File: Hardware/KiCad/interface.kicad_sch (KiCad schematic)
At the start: 36 parts, among them J1 USB_C, J2 STLink, J6 UART, J7 OLED, SW10 SW_Push_45deg, SW11 SW_Push_45deg, SW12 SW_Push_45deg, SW13 SW_Push_45deg, SW14 SW_Push_45deg, SW15 SW_Push_45deg, SW16 SW_Push_45deg, SW17 SW_Push_45deg, SW18 Channel Select - ACZ11BRXE, SW2 SW_Push_45deg, SW3 SW_Push_45deg, SW4 SW_Push_45deg, SW5 SW_Push_45deg, SW6 SW_Push_45deg, SW7 SW_Push_45deg, SW8 SW_Push_45deg, SW9 SW_Push_45deg, U1 USBLC6-2

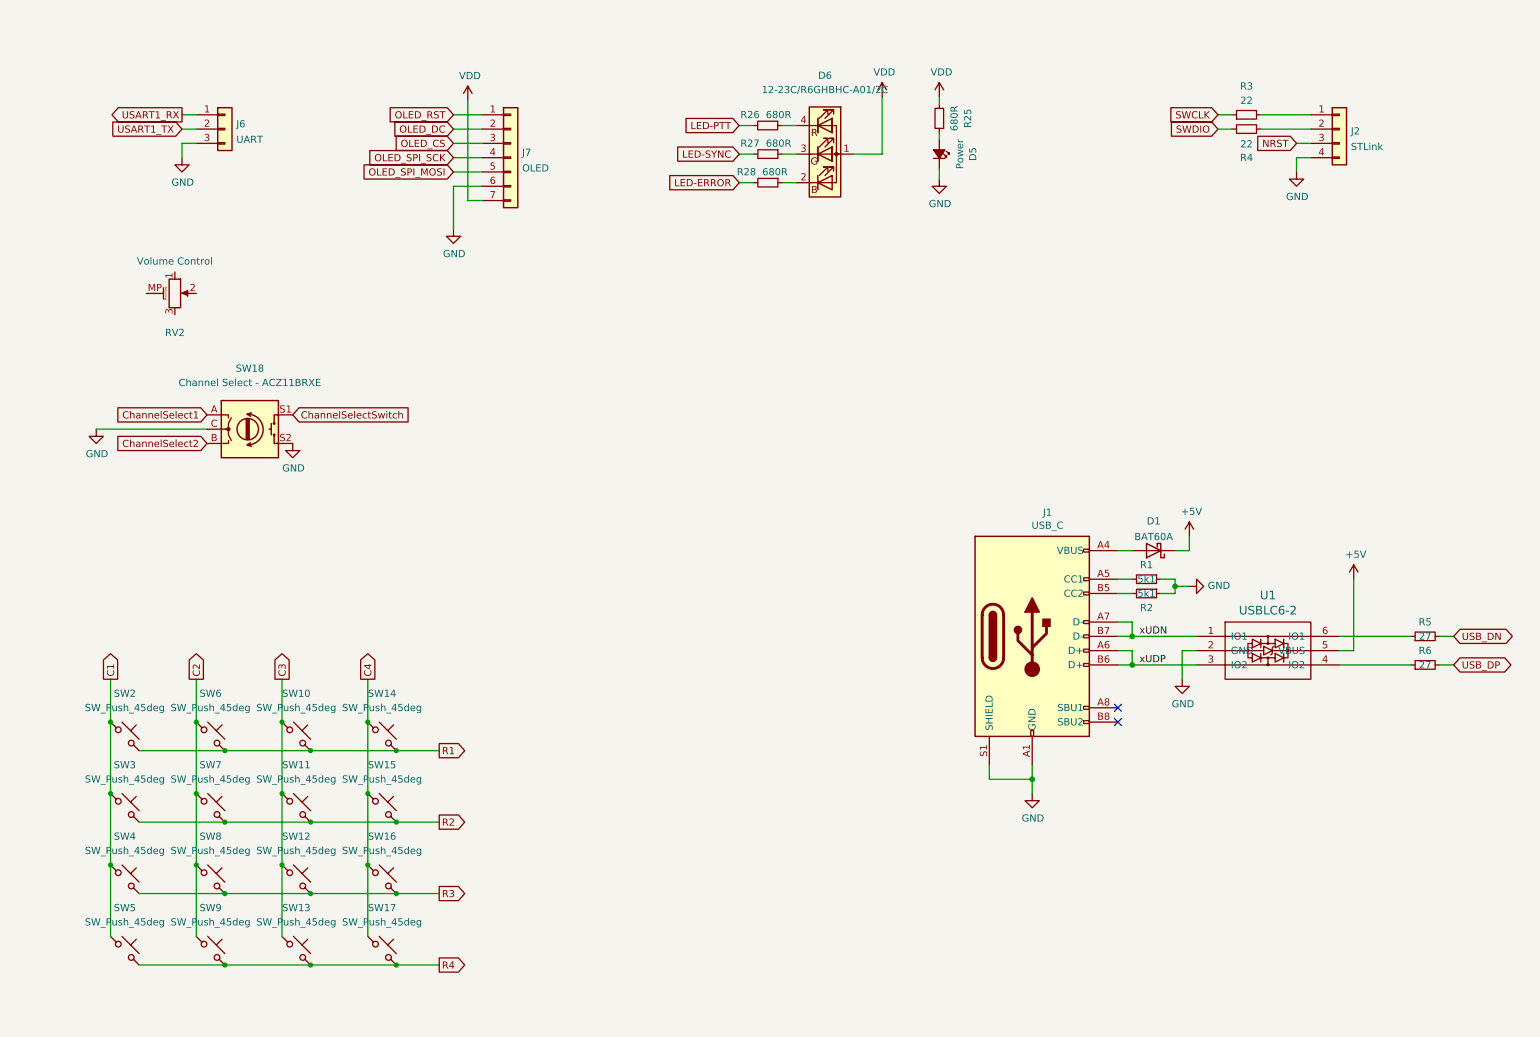
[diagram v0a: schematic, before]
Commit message: Schematic update
- nets for the internal speaker renamed
- encoder nets renamed, encoder circuit updated
- various other minor edits
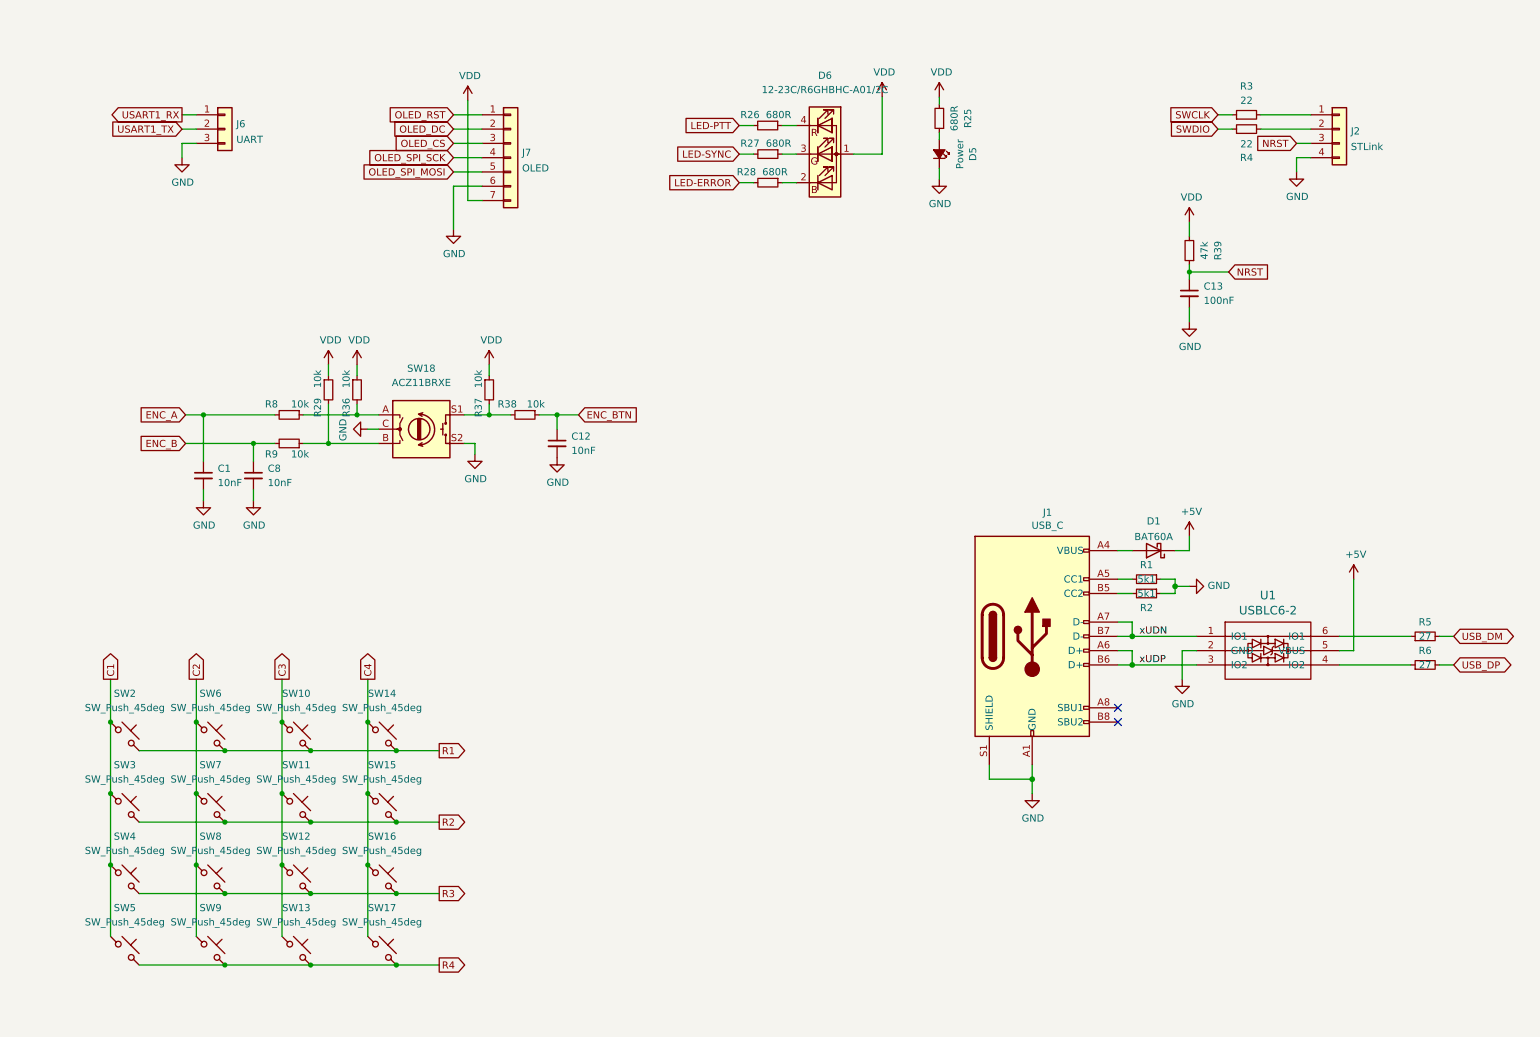
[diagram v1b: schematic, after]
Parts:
- removed RV2: Volume Control, Potentiometer_THT:Potentiometer_Alps_RK09L_Single_Horizontal, symbol Device:R_Potentiometer_MountingPin
- added C1, C12, C8: 10nF, Capacitor_SMD:C_0402_1005Metric, symbol Device:C_Small
- added C13: 100nF, Capacitor_SMD:C_0402_1005Metric, symbol Device:C_Small
- added R29, R36, R37, R38, R8, R9: 10k, Resistor_SMD:R_0402_1005Metric, symbol pkl_device:pkl_R_Small
- added R39: 47k, Resistor_SMD:R_0402_1005Metric, symbol pkl_device:pkl_R_Small
- SW18: value Channel Select - ACZ11BRXE -> ACZ11BRXE
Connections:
- net GND: now also C1.2, C12.2, C13.2, C8.2
- net NRST: now also C13.1, R39.1
- net VDD: now also R29.1, R36.1, R37.1, R39.2
- net ChannelSelect1: no longer names the net of SW18.A
- net ChannelSelect1: now also R36.2, R8.1
- net ChannelSelect2: no longer names the net of SW18.B
- net ChannelSelect2: now also R29.2, R9.1
- net ChannelSelectSwitch: no longer names the net of SW18.S1
- net ChannelSelectSwitch: now also R37.2, R38.2
- net USB_DN renamed USB_DM
- new net ENC_A: C1.1, R8.2
- new net ENC_B: C8.1, R9.2
- new net ENC_BTN: C12.1, R38.1
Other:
- moved on the sheet: SW18

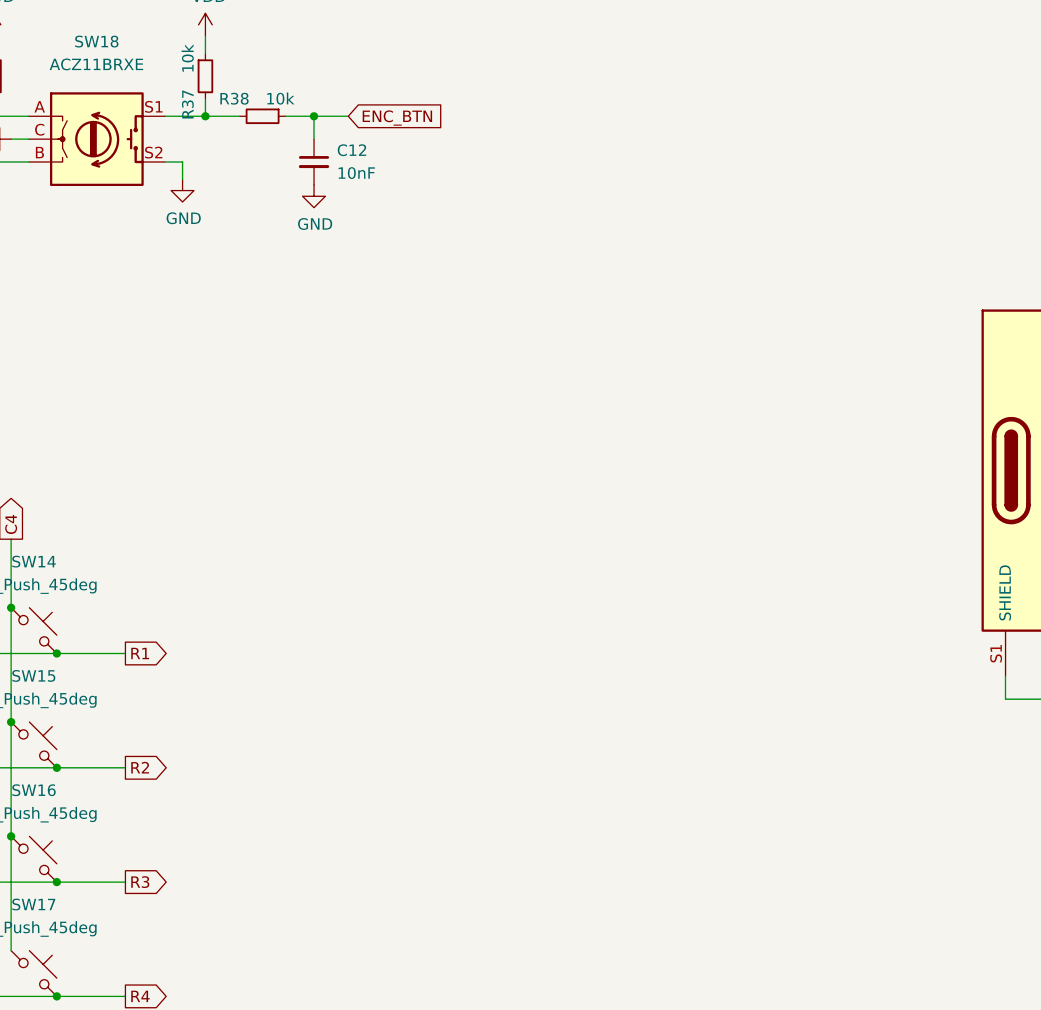
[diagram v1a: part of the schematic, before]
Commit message: Additional function buttons - F1, F2
Closes #24
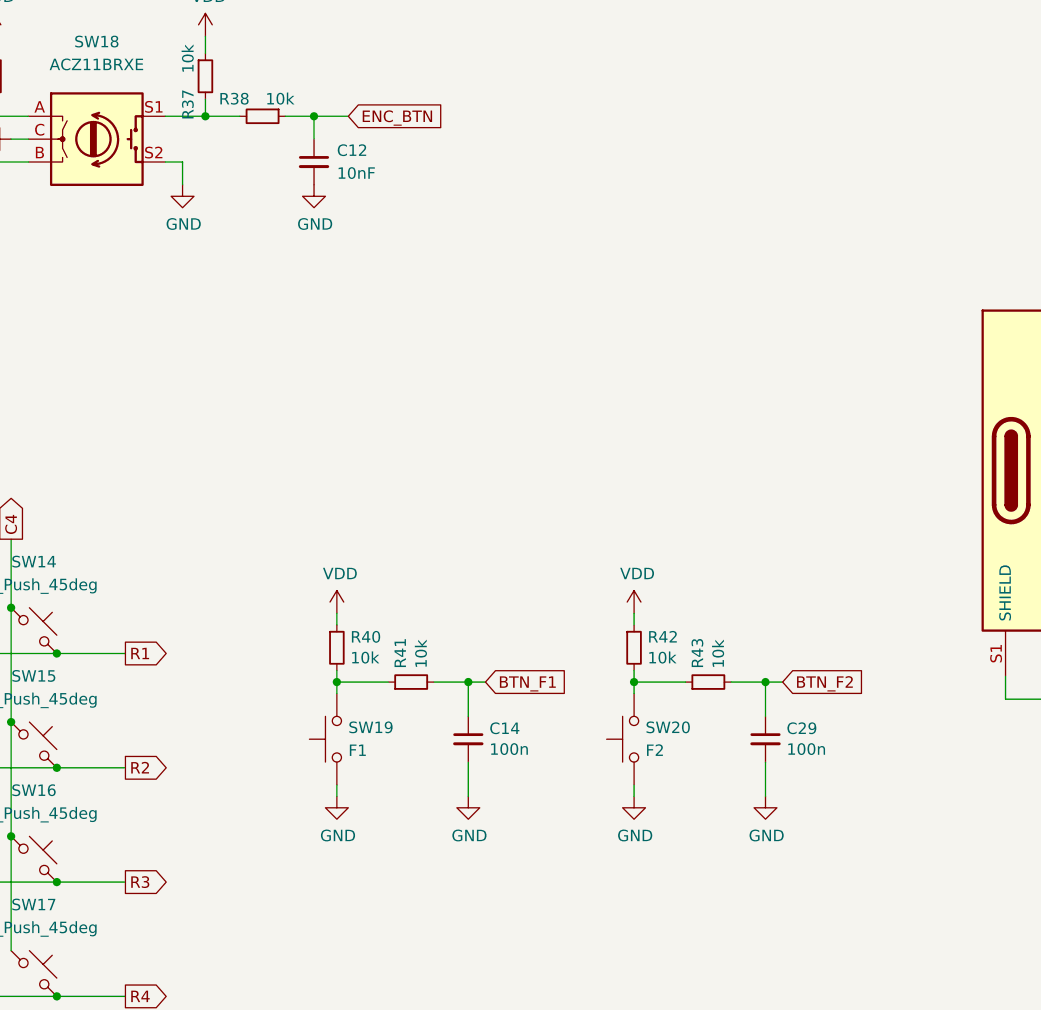
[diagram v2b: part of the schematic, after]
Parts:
- added C14, C29: 100n, Capacitor_SMD:C_0402_1005Metric, symbol pkl_device:pkl_C_Small
- added R40, R41, R42, R43: 10k, Resistor_SMD:R_0402_1005Metric, symbol pkl_device:pkl_R_Small
- added SW19: F1, Button_Switch_THT:SW_Tactile_SPST_Angled_PTS645Vx31-2LFS, symbol Switch:SW_Push
- added SW20: F2, Button_Switch_THT:SW_Tactile_SPST_Angled_PTS645Vx31-2LFS, symbol Switch:SW_Push
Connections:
- net GND: now also C14.2, C29.2, SW19.1, SW20.1
- net VDD: now also R40.1, R42.1
- new net: R40.2, R41.1, SW19.2
- new net: R42.2, R43.1, SW20.2
- new net BTN_F1: C14.1, R41.2
- new net BTN_F2: C29.1, R43.2

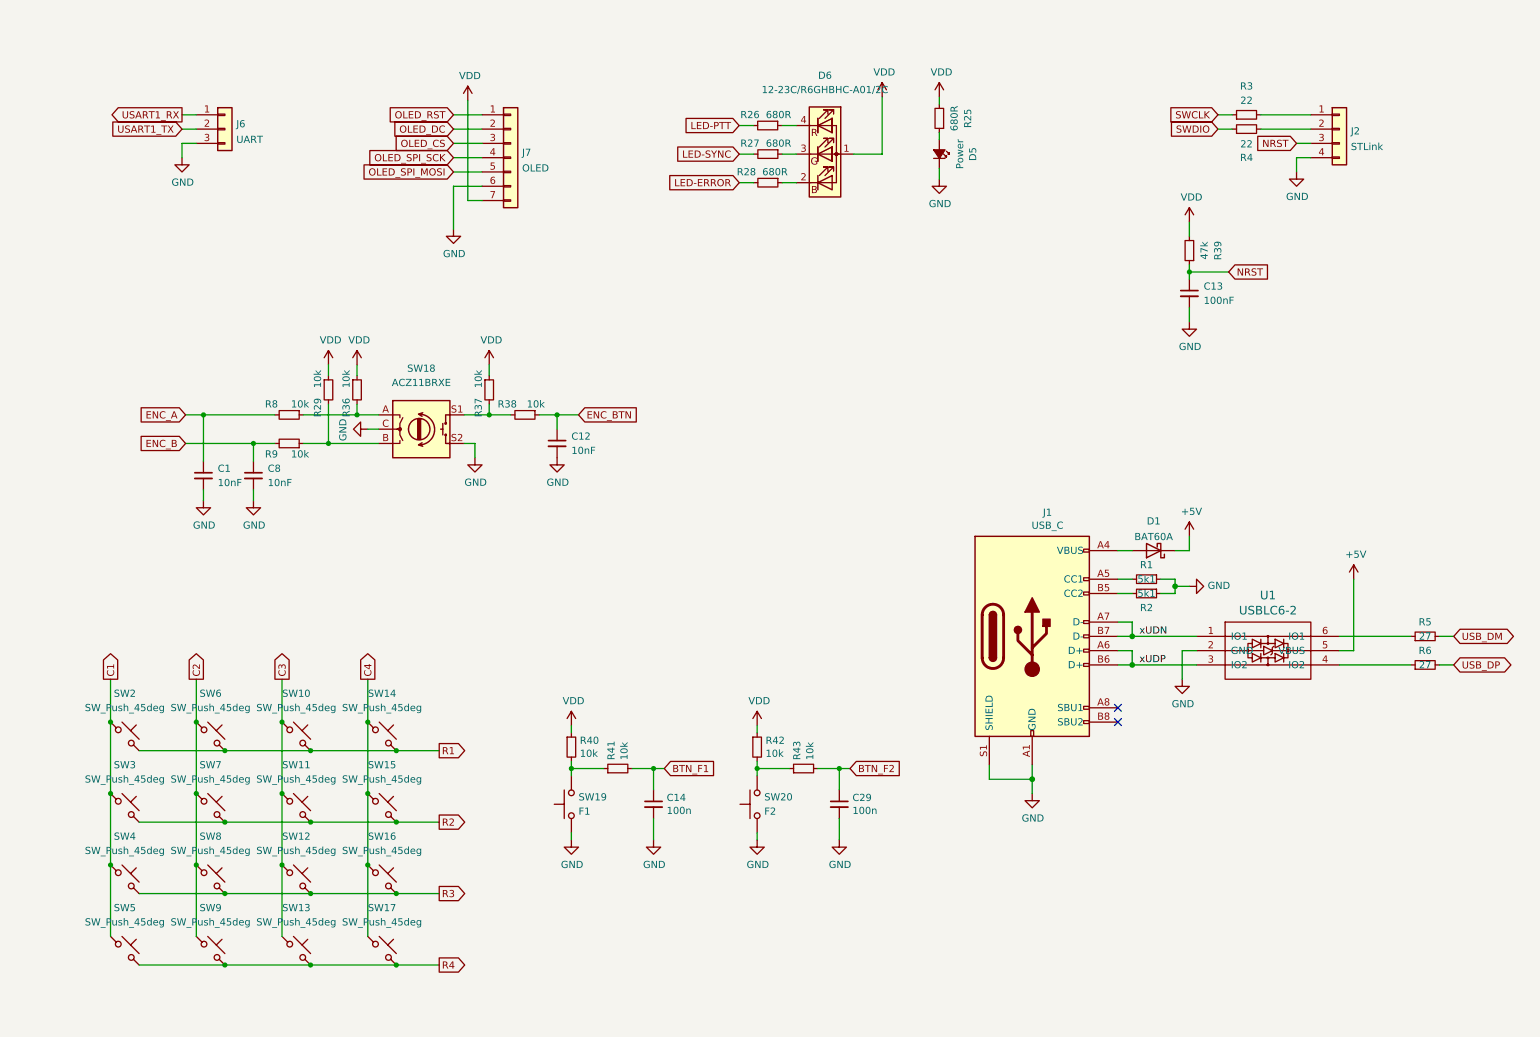
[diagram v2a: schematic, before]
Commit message: add fpc display board connector, move components around, rough size of board
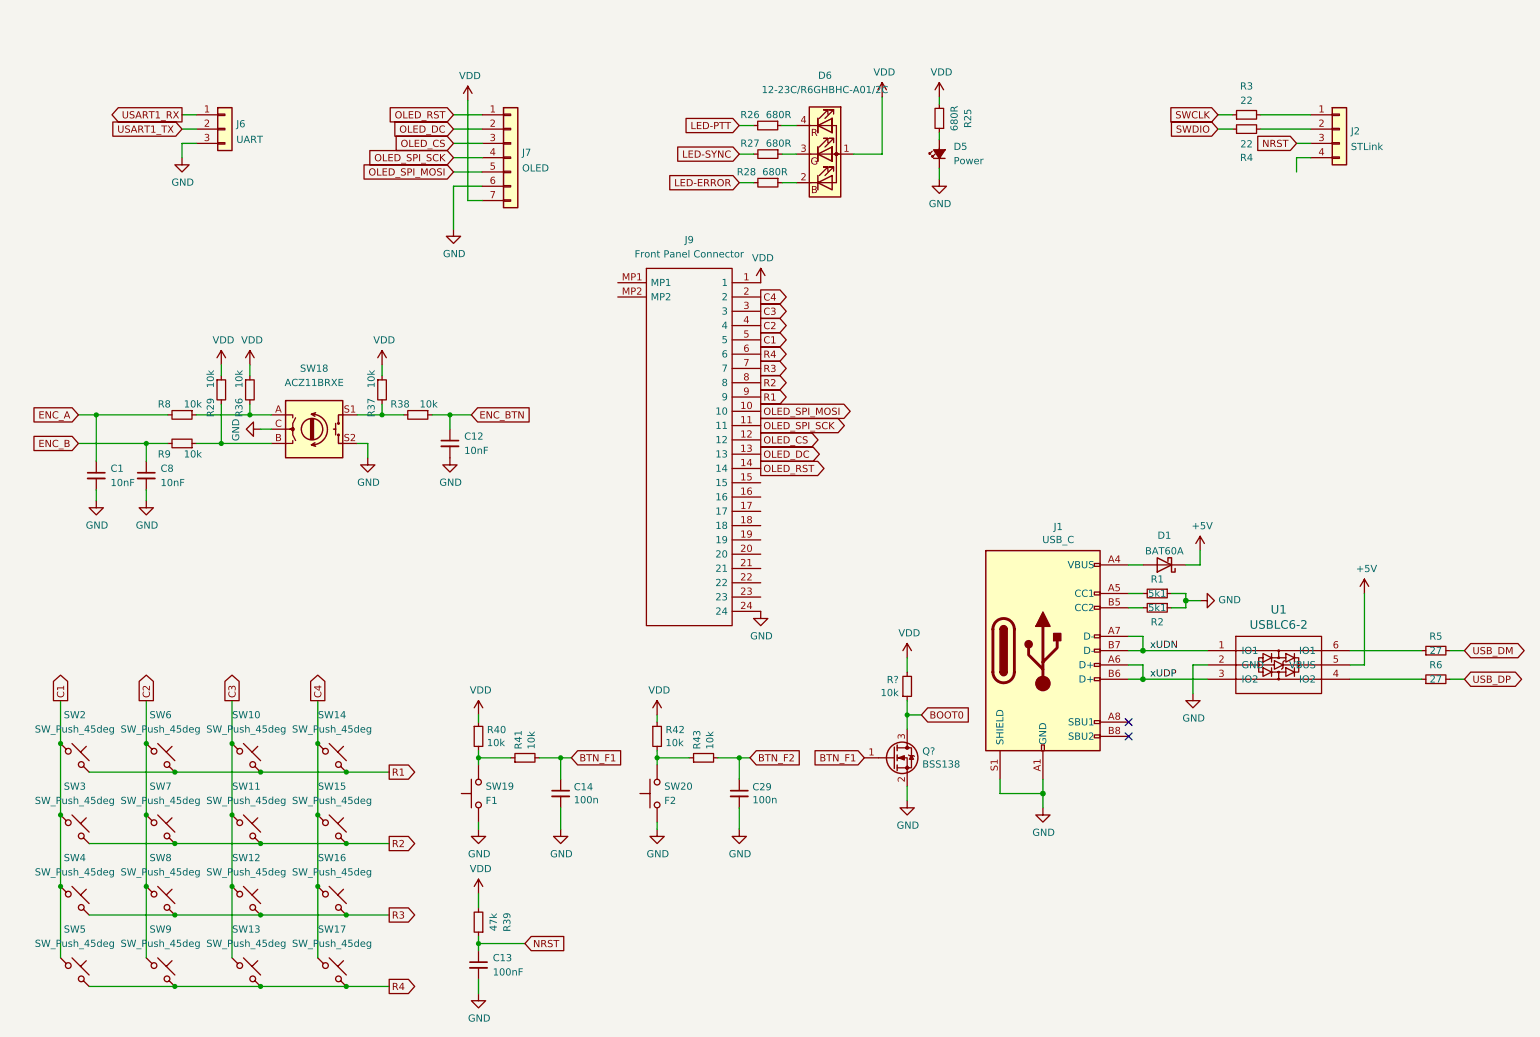
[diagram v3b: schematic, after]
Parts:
- removed D5: Power, Diode_SMD:D_0201_0603Metric, symbol pkl_device:pkl_Led_Small
- added D5: Power, Diode_SMD:D_0201_0603Metric, symbol Device:LED_Small_Filled
- added J9: Front Panel Connector, FH19SC24S05SH09, symbol SamacSys_Parts2:FH19SC-24S-0.5SH_09_
- added Q?: BSS138, Package_TO_SOT_SMD:SOT-23, symbol Mainboard-rescue:BSS138-Transistor_FET
- added R?: 10k, Resistor_SMD:R_0603_1608Metric, symbol Mainboard-rescue:R_Small-Device
- J1: footprint Connector_USB:USB_C_Receptacle_HRO_TYPE-C-31-M-12 -> Connector_USB:USB_C_Receptacle_GCT_USB4085
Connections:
- net BTN_F1: now also Q?.1 (G)
- net C1: now also J9.5
- net C2: now also J9.4
- net C3: now also J9.3
- net C4: now also J9.2
- net GND: now also D5.1 (K), J9.24, Q?.2 (S); no longer J2.4 (Pin_4)
- net OLED_CS: now also J9.12
- net OLED_DC: now also J9.13
- net OLED_RST: now also J9.14
- net OLED_SPI_MOSI: now also J9.10
- net OLED_SPI_SCK: now also J9.11
- net R1: now also J9.9
- net R2: now also J9.8
- net R3: now also J9.7
- net R4: now also J9.6
- net VDD: now also J9.1, R?.2
- net at R25.1: now also D5.2 (A)
- new net BOOT0: Q?.3 (D), R?.1
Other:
- moved on the sheet: C1, C12, C13, C14, C29, C8, D1, J1, R1, R2, R29, R36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
